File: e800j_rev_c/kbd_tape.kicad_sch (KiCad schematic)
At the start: 66 parts, among them J30 Conn_01x01_Socket, J31 Conn_01x01_Socket, J32 Conn_01x01_Socket, J33 Conn_01x01_Socket, J34 Conn_01x01_Socket, J35 Conn_01x01_Socket, J36 Conn_01x01_Socket, T4 BC307, T5 BC307, U4 74LS04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

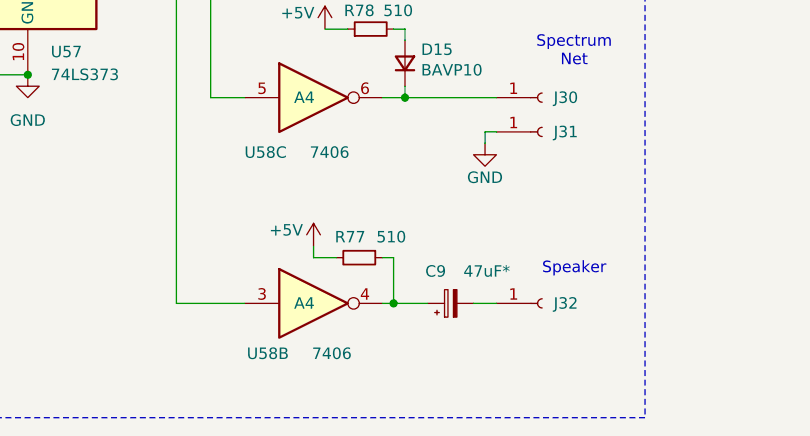
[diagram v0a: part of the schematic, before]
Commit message: Marked unpopulated components properly (see #14)
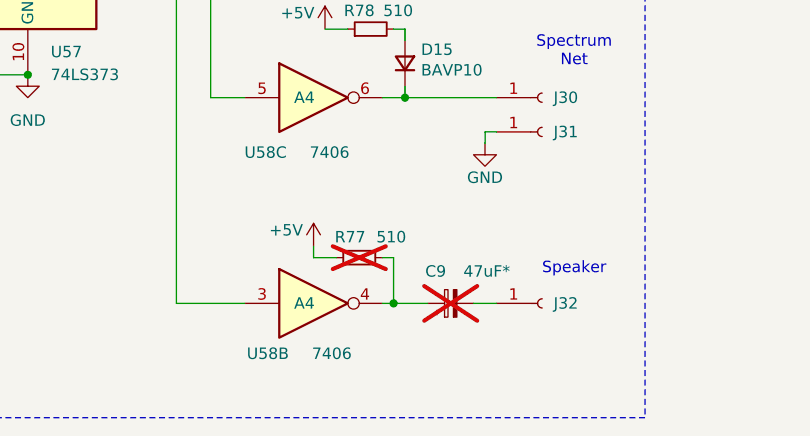
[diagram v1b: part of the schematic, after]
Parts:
- C9: now not fitted
- R77: now not fitted; now left out of the parts list
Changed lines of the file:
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@@
 		(unit 1)
 		(exclude_from_sim no)
-		(in_bom yes)
+		(in_bom no)
 		(on_board yes)
-		(dnp no)
+		(dnp yes)
 		(property "Reference" "R77"
 			(at 100.584 170.434 90)
@@
 		(in_bom no)
 		(on_board yes)
-		(dnp no)
+		(dnp yes)
 		(property "Reference" "C9"
 			(at 111.252 174.244 90)
